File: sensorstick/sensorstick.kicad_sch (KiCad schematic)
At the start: 20 parts, among them J1 USB-A Header, U1 ESP32-C3_SUPERMINI, U2 SGP30, U3 SHT4x, U4 SCD40-D-R2, U5 PCA9306DC, U6 LP5907MFX-1.8

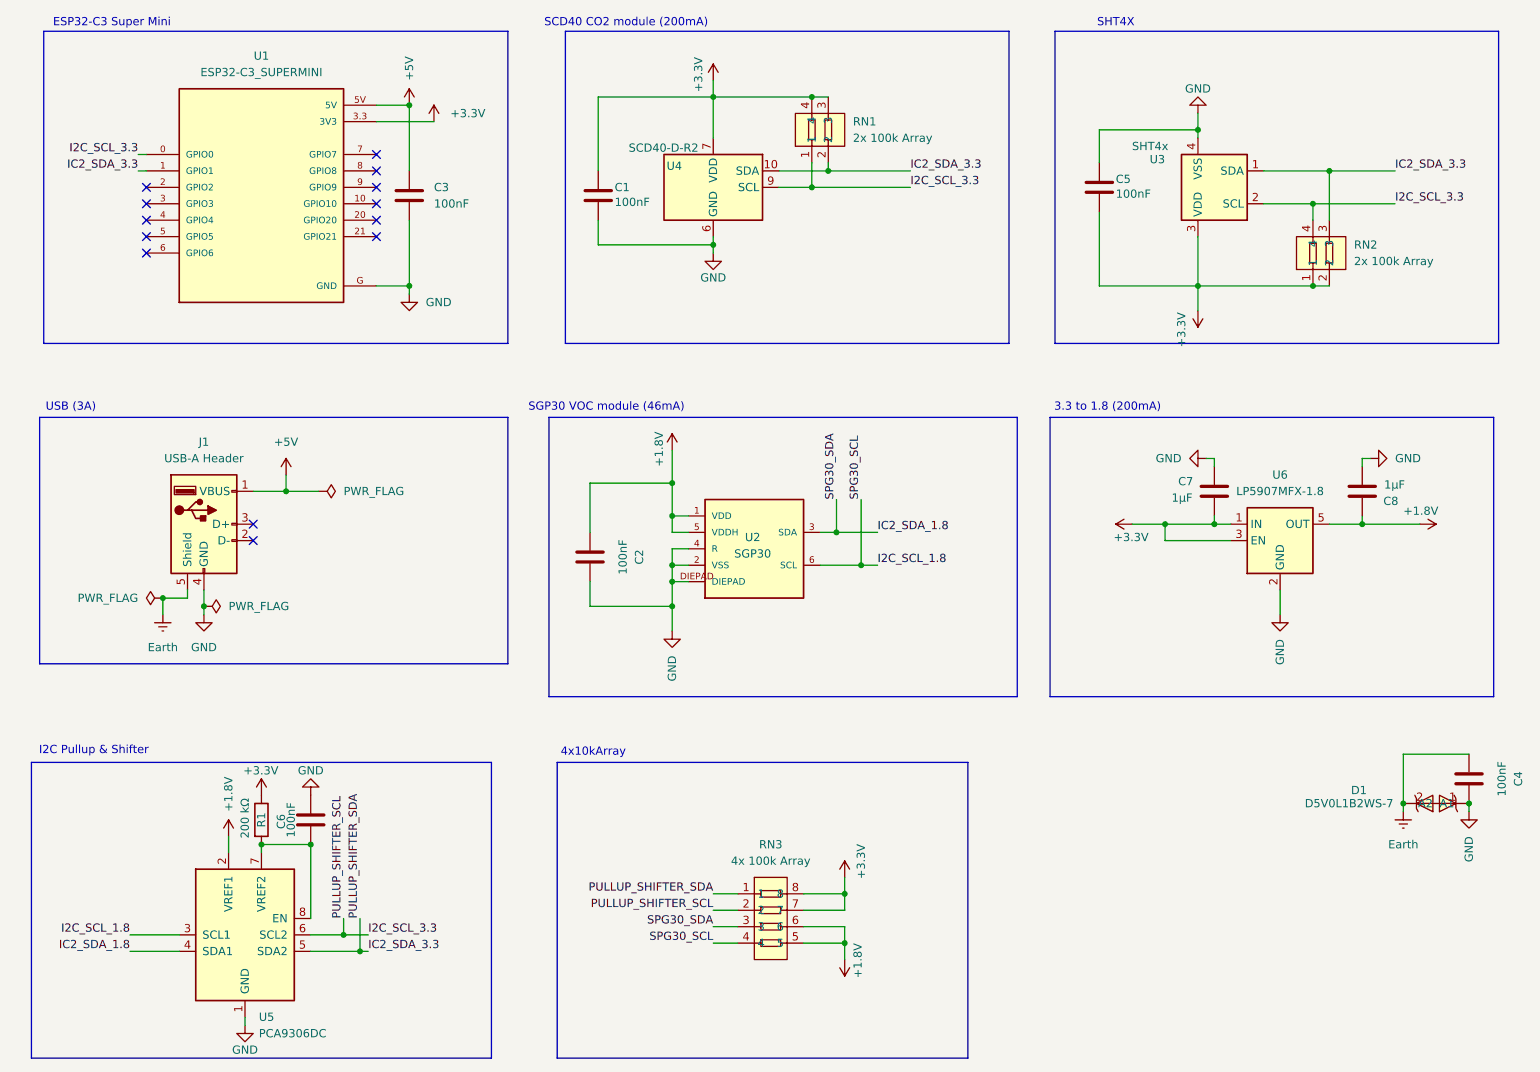
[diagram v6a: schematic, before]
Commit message: added NTC for board Temperature and finaly touch bevore ordering the PCB
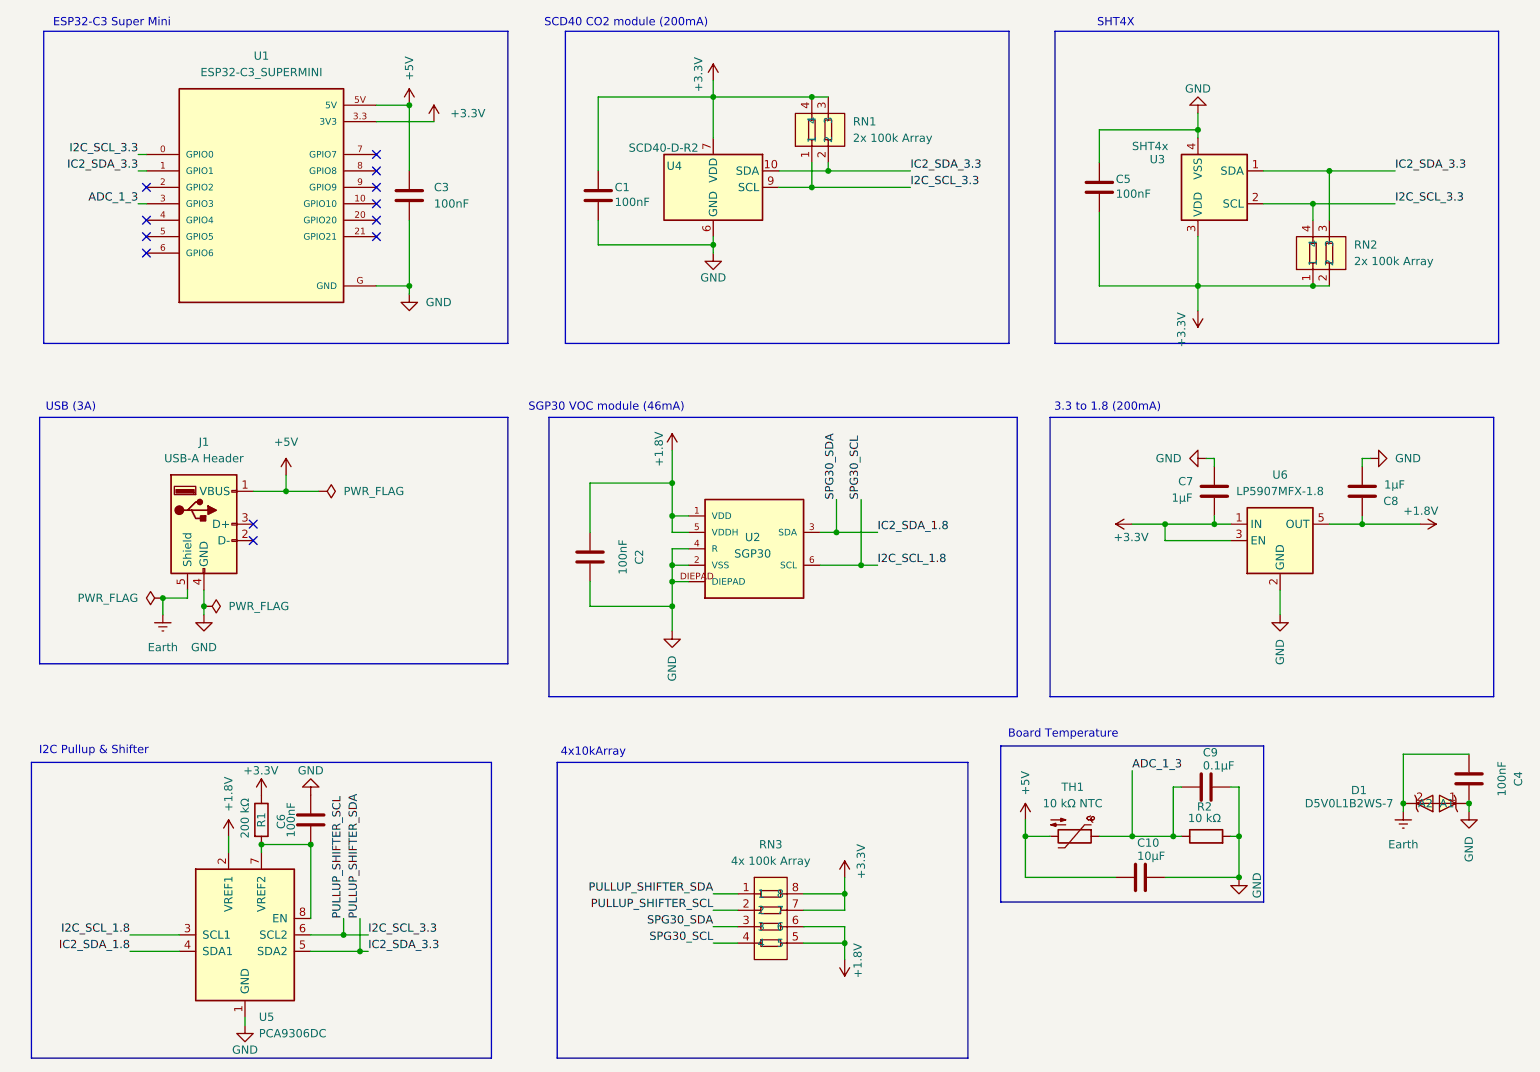
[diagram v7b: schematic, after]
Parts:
- added C10: 10µF, Capacitor_SMD:C_0603_1608Metric, symbol Device:C
- added C9: 0.1µF, Capacitor_SMD:C_0603_1608Metric, symbol Device:C
- added R2: 10 kΩ, Resistor_SMD:R_0603_1608Metric, symbol Device:R
- added TH1: 10 kΩ NTC, Resistor_SMD:R_0603_1608Metric, symbol Device:Thermistor_NTC
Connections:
- net +5V: now also C10.1, TH1.2
- net GND: now also C10.2, C9.2, R2.2
- net ADC_1_3: now reaches U1.3 (GPIO3)
- net ADC_1_3: now also C9.1, R2.1, TH1.1
- no-connect marks 13 -> 12
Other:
- note added: "Board Temperature"

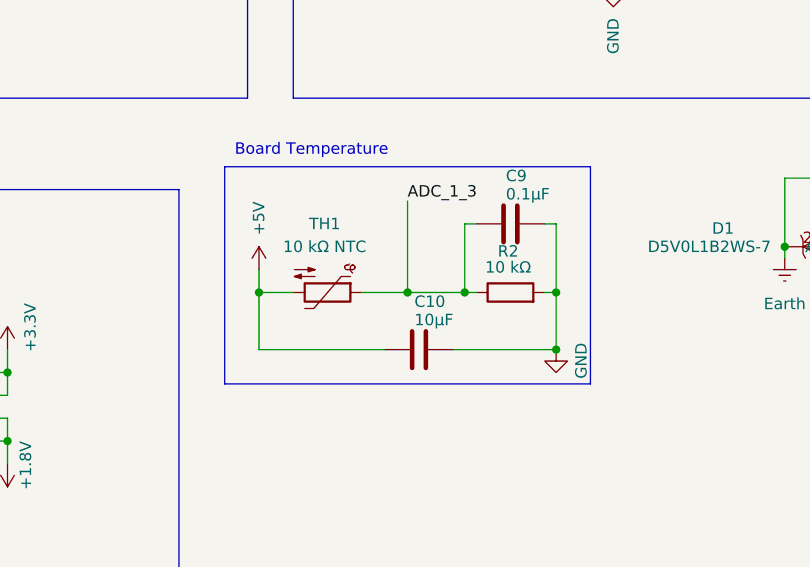
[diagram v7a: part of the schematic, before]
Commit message: changed ntc values
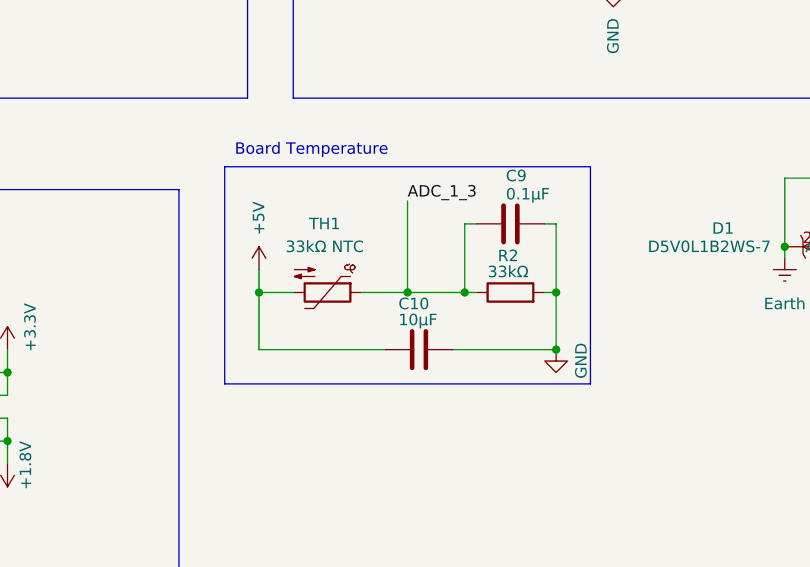
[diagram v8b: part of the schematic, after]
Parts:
- R2: value 10 kΩ -> 33kΩ
- TH1: value 10 kΩ NTC -> 33kΩ NTC
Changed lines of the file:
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@@
 		(dnp no)
 		(property "Reference" "C10"
-			(at 198.882 154.686 90)
+			(at 197.104 154.94 90)
 			(effects
 				(font
@@
 		)
 		(property "Value" "10µF"
-			(at 198.882 156.718 90)
+			(at 197.104 156.718 90)
 			(effects
 				(font
@@
 			)
 		)
-		(property "Value" "10 kΩ NTC"
+		(property "Value" "33kΩ NTC"
 			(at 188.9125 148.59 90)
 			(effects
@@
 		(dnp no)
 		(property "Reference" "R2"
-			(at 209.296 149.098 90)
+			(at 209.296 149.606 90)
 			(effects
 				(font
@@
 			)
 		)
-		(property "Value" "10 kΩ"
-			(at 209.296 150.876 90)
+		(property "Value" "33kΩ"
+			(at 209.296 151.384 90)
 			(effects
 				(font
